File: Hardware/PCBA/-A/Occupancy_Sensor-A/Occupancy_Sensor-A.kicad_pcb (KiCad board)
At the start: 2 copper layers, 30 x 30 mm, 68 parts, among them J1 USB_C_Receptacle, J2 Conn_02x05_Odd_Even, Q1 2N7002, Q2 2N7002, Q3 2N7002, Q4 2N7002, Q5 2N7002, SW1 SW_Push, SW2 SW_SPDT, U1 TCS3430, U2 VL53L8CX, U4 STM32WB55CGUx, U6 ECMF02-2AMX6, U8 TPS7A03185PDQNR, U9 TPS7A0333PDBVR, Y2 Crystal_GND24_Small

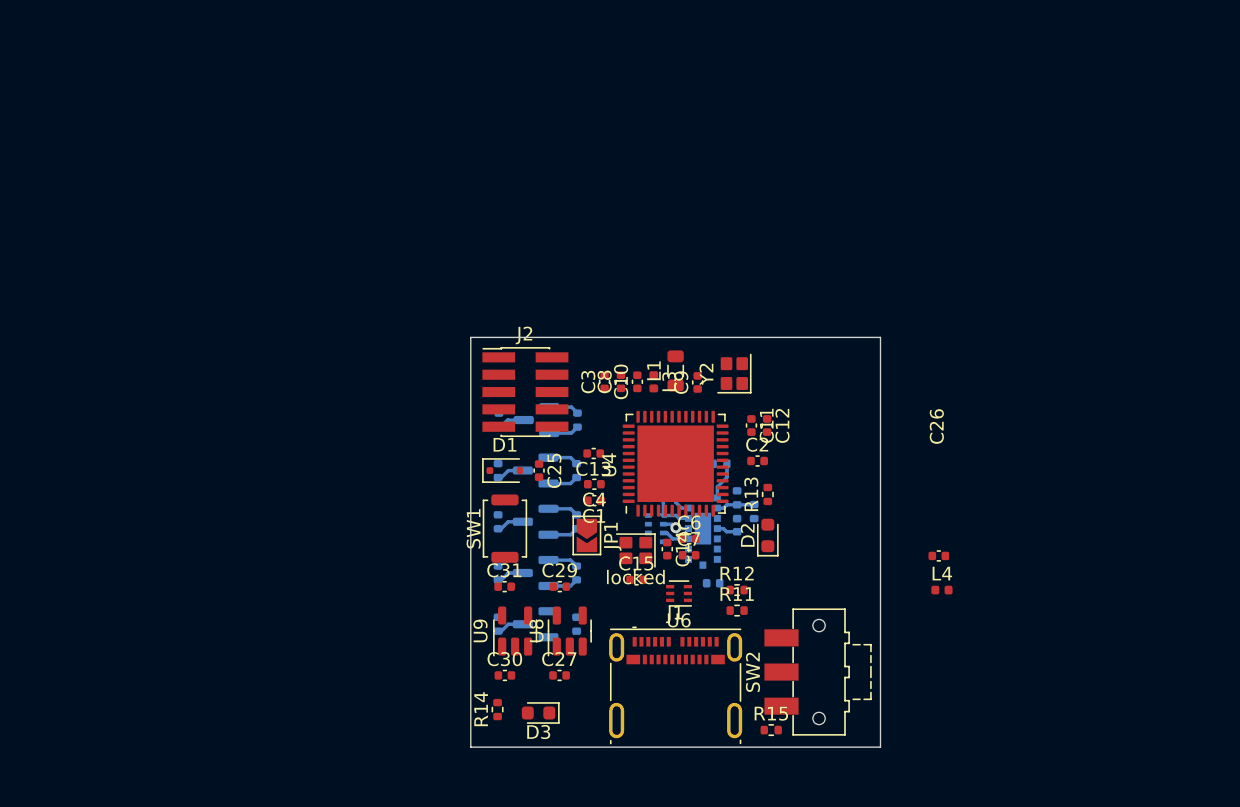
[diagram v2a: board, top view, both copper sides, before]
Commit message: General layout, footprint fixes
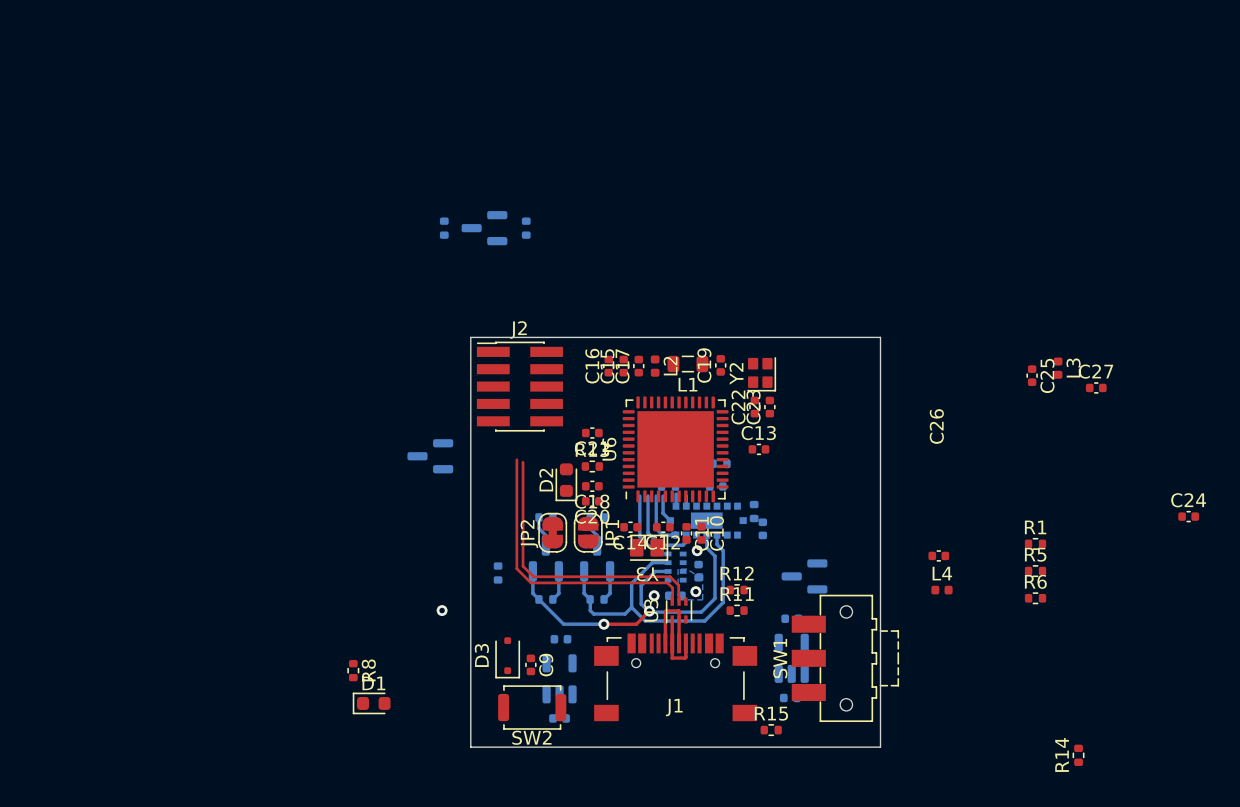
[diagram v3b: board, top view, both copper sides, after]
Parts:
- removed C29, C30, C31: 1u, Capacitor_SMD:C_0402_1005Metric
- removed R21, R22, R23, R24, R25: 2.2K, Resistor_SMD:R_0402_1005Metric
- removed U8: TPS7A03185PDQNR, Package_TO_SOT_SMD:SOT-23-5
- removed U9: TPS7A0333PDBVR, Package_TO_SOT_SMD:SOT-23-5
- removed locked: Crystal_GND24_Small, Crystal:Crystal_SMD_SeikoEpson_FA128-4Pin_2.0x1.6mm
- added C19: 4.7u, Capacitor_SMD:C_0402_1005Metric, F.Cu at (148.3, 102.0)
- added C20: 100n, Capacitor_SMD:C_0402_1005Metric, F.Cu at (138.9, 112.0)
- added C21: 100n, Capacitor_SMD:C_0402_1005Metric, F.Cu at (138.9, 107.0)
- added C22: 100n, Capacitor_SMD:C_0402_1005Metric, F.Cu at (150.8, 105.1)
- added C23: 100p, Capacitor_SMD:C_0402_1005Metric, F.Cu at (151.9, 105.1)
- added C24: 0.8pf, Capacitor_SMD:C_0402_1005Metric, F.Cu at (182.6, 113.1)
- added JP2: Jumper_2_Bridged, Jumper:SolderJumper-2_P1.3mm_Bridged_RoundedPad1.0x1.5mm, F.Cu at (136.0, 114.3)
- added L2: 10n, Inductor_SMD:L_0402_1005Metric, F.Cu at (143.5, 102.1)
- added R1: 5.1K, Resistor_SMD:R_0402_1005Metric, F.Cu at (171.3, 115.1)
- added R18: 2.2K, Resistor_SMD:R_0402_1005Metric, B.Cu at (139.2, 113.2)
- added R19: 2.2K, Resistor_SMD:R_0402_1005Metric, B.Cu at (135.5, 119.2)
- added R5: 47K, Resistor_SMD:R_0402_1005Metric, F.Cu at (171.3, 117.1)
- added R6: 47K, Resistor_SMD:R_0402_1005Metric, F.Cu at (171.3, 119.1)
- added U3: ECMF02-2AMX6, Package_DFN_QFN:ST_UQFN-6L_1.5x1.7mm_P0.5mm, F.Cu at (145.2, 120.0)
- added U5: TCS3430, Occupancy_Sensor_Custom_Footprints:TCS3430, B.Cu at (145.0, 116.8)
- added Y3: NX2012_32K768, Occupancy_Sensor_Custom_Footprints:NX2012_32K768, F.Cu at (142.9, 115.4)
- C1: value 100n -> 4.7u; moved to B.Cu
- C10: value 100n -> 1u
- C11: value 100n -> 10n
- C12: value 100p -> 10p
- C13: value 100n -> 4.7u
- C15: value 10p -> 4.7u
- C16, C17: moved to F.Cu
- C18: value 1u -> 100n; moved to F.Cu
- C2, C6: moved to B.Cu
- C25: value 100n -> 0.3pf
- C26: value C_Small -> 10nf
- C27: value 1u -> 1.2pf
- C3: value 100n -> 1u; moved to B.Cu
- C4: value 4.7u -> 100n; moved to B.Cu
- C5: value 4.7u -> 1u
- C7: value 10n -> 1u; moved to B.Cu
- C8: value 4.7u -> 1u; moved to B.Cu
- C9: value 4.7u -> 100n
- D1: value BAT54J -> LED; footprint Diode_SMD:D_SOD-323F -> LED_SMD:LED_0603_1608Metric
- D3: value LED -> BAT54J; footprint LED_SMD:LED_0603_1608Metric -> Diode_SMD:D_SOD-323F
- J1: footprint Connector_USB:USB_C_Receptacle_Molex_105450-0101 -> Occupancy_Sensor_Custom_Footprints:TYPEC-304S-ACP16
- JP1: footprint Jumper:SolderJumper-2_P1.3mm_Open_TrianglePad1.0x1.5mm -> Jumper:SolderJumper-2_P1.3mm_Open_RoundedPad1.0x1.5mm
- R10, R3: value 40K -> 47K
- R11: value 5.1K -> 40K
- R12: value 5.1K -> 47K
- R14: value 1K -> 2.2K
- R16, R17: value 47K -> 2.2K
- R2: value 47K -> 5.1K
- R4: value 47K -> 40K
- R8: value 47K -> 1K; moved to F.Cu
- SW1: value SW_Push -> SW_SPDT; footprint Button_Switch_SMD:SW_Push_SPST_NO_Alps_SKRK -> Button_Switch_SMD:SW_SPDT_CK-JS102011SAQN
- SW2: value SW_SPDT -> SW_Push; footprint Button_Switch_SMD:SW_SPDT_CK-JS102011SAQN -> Button_Switch_SMD:SW_Push_SPST_NO_Alps_SKRK
- U1: value TCS3430 -> TPS7A0333PDBVR; footprint Occupancy_Sensor_Custom_Footprints:TCS3430 -> Package_TO_SOT_SMD:SOT-23-5
- U4: value STM32WB55CGUx -> TPS7A03185PDQNR; footprint Package_DFN_QFN:QFN-48-1EP_7x7mm_P0.5mm_EP5.6x5.6mm -> Package_TO_SOT_SMD:SOT-23-5; moved to B.Cu
- U6: value ECMF02-2AMX6 -> STM32WB55CGUx; footprint Package_DFN_QFN:ST_UQFN-6L_1.5x1.7mm_P0.5mm -> Package_DFN_QFN:QFN-48-1EP_7x7mm_P0.5mm_EP5.6x5.6mm
- Y2: value Crystal_GND24_Small -> NX2016SA_32M; footprint Crystal:Crystal_SMD_SeikoEpson_FA128-4Pin_2.0x1.6mm -> Occupancy_Sensor_Custom_Footprints:NX2016SA_32M
- moved C27 44.6 mm to (175.8, 103.7)
- moved R14 42.7 mm to (174.5, 130.6)
- moved C25 36.8 mm to (171.1, 102.8)
- moved L3 29.6 mm to (173.0, 102.2)
- moved R7 29.2 mm to (134.1, 92.0)
- moved R10 29.1 mm to (128.1, 92.0)
- moved SW1 26.7 mm to (157.5, 123.5)
- moved C3 24.9 mm to (136.5, 127.9), turned to 0 degrees
- moved C9 24.0 mm to (134.4, 124.0), turned to -90 degrees
- moved SW2 21.2 mm to (134.5, 127.1), turned to 180 degrees
- moved Q3 20.0 mm to (154.4, 117.5)
- moved D1 19.6 mm to (122.9, 126.8)
- moved C17 16.8 mm to (142.3, 102.1), turned to 90 degrees
- moved U4 16.6 mm to (153.5, 123.5)
- moved C8 16.2 mm to (145.0, 118.9), turned to 0 degrees
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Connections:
- C1 pad 1: VDD -> +3.3V
- C10 pad 1: VDD -> VDD_ANALOG
- C11 pad 1: VDD -> VDD_ANALOG
- C12 pad 1: VDD -> GND
- C12 pad 2: GND -> /OSC32_OUT
- C13 pad 1: VDD_USB -> +3.3V
- C14 pad 1: GND -> /OSC32_IN
- C14 pad 2: /OSC32_OUT -> GND
- C15 pad 1: /OSC32_OUT -> +3.3V
- C16 pad 1: +1V8 -> +3.3V
- C17 pad 1: +1V8 -> +3.3V
- C18 pad 1: +1V8 -> +3.3V
- C2 pad 1: VDD -> +1V8
- C25 pad 1: NRST -> Net-(C25-Pad1)
- C26 pad 1: unconnected-(C26-Pad1) -> Net-(C26-Pad1)
- C26 pad 2: unconnected-(C26-Pad2) -> Net-(C26-Pad2)
- C27 pad 1: VBUS -> Net-(AE1-A)
- C3 pad 1: VDD -> VBUS
- C4 pad 1: VDD -> +1V8
- C6 pad 1: VDD_ANALOG -> VBUS
- C7 pad 1: VDD_ANALOG -> +1V8
- C8 pad 1: VDD -> +1V8
- C9 pad 1: Net-(U4-VFBSMPS) -> NRST
- D1 pad 1: Net-(D1-K) -> GND
- D1 pad 2: NRST -> Net-(D1-A)
- D3 pad 1: GND -> Net-(D3-K)
- D3 pad 2: Net-(D3-A) -> NRST
- J1 pad A6: Net-(U6-D+_in) -> Net-(U3-D+_in)
- J1 pad A7: Net-(U6-D-_in) -> Net-(U3-D-_in)
- J1 pad B6: Net-(U6-D+_in) -> Net-(U3-D+_in)
- J1 pad B7: Net-(U6-D-_in) -> Net-(U3-D-_in)
- JP1 pad 1: VDD -> +3.3V
- L1 pad 1: Net-(U4-VFBSMPS) -> Net-(U6-VFBSMPS)
- Q1 pad 2: /INT_CLR_1V8 -> /INT_TOF_1V8
- Q1 pad 3: /INT_CLR -> /INT_TOF
- Q2 pad 2: /SCL_1V8 -> /SYNC_1V8
- Q2 pad 3: /SCL_3V3 -> /SYNC_3V3
- Q3 pad 2: /SYNC_1V8 -> /INT_CLR_1V8
- Q3 pad 3: /SYNC_3V3 -> /INT_CLR
- Q4 pad 2: /SDA_1V8 -> /SCL_1V8
- Q4 pad 3: /SDA_3V3 -> /SCL_3V3
- Q5 pad 2: /INT_TOF_1V8 -> /SDA_1V8
- Q5 pad 3: /INT_TOF -> /SDA_3V3
- R10 pad 1: /I2C_RST -> +3.3V
- R10 pad 2: /I2C_RST_1V8 -> /SYNC_3V3
- R11 pad 1: Net-(J1-CC1) -> /LPn
- R11 pad 2: GND -> /LPn_1V8
- R12 pad 1: Net-(J1-CC2) -> /LPn_1V8
- R14 pad 1: Net-(D3-A) -> +1V8
- R14 pad 2: VBUS -> /INT_CLR_1V8
- R15 pad 1: Net-(SW2-B) -> Net-(SW1-B)
- R16 pad 2: /INT_TOF_1V8 -> /SCL_1V8
- R17 pad 2: /INT_TOF -> /INT_CLR
- R2 pad 1: Net-(U2-SPI_I2C_N) -> Net-(J1-CC2)
- R20 pad 1: +1V8 -> +3.3V
- R20 pad 2: /INT_CLR_1V8 -> /SDA_3V3
- R3 pad 1: /LPn -> Net-(U2-SPI_I2C_N)
- R3 pad 2: /LPn_1V8 -> GND
- R4 pad 1: /LPn_1V8 -> /I2C_RST
- R4 pad 2: GND -> /I2C_RST_1V8
- R8 pad 1: +3.3V -> Net-(D1-A)
- R8 pad 2: /SYNC_3V3 -> VBUS
- R9 pad 1: /I2C_RST_1V8 -> +3.3V
- R9 pad 2: GND -> /INT_TOF
- SW1 pad 1: GND -> +3.3V
- SW1 pad 2: Net-(D1-K) -> Net-(SW1-B)
- SW2 pad 1: +3.3V -> GND
- SW2 pad 2: Net-(SW2-B) -> Net-(D3-K)
- U1 pad 1: +1V8 -> VBUS
- U1 pad 2: /SDA_1V8 -> GND
- U1 pad 3: /SCL_1V8 -> VBUS
- U1 pad 4: /INT_CLR_1V8 -> unconnected-(U1-NC-Pad4)
- U1 pad 5: unconnected-(U1-N/C-Pad5) -> +3.3V
- U4 pad 1: Net-(JP1-B) -> VBUS
- U4 pad 2: /OSC32_IN -> GND
- U4 pad 3: /OSC32_OUT -> /1V8_EN
- U4 pad 4: BOOT -> unconnected-(U4-NC-Pad4)
- U4 pad 5: /PB8 -> +1V8
- U6 pad 1: Net-(U6-D+_in) -> Net-(JP1-B)
- U6 pad 2: Net-(U6-D-_in) -> /OSC32_IN
- U6 pad 3: GND -> /OSC32_OUT
- U6 pad 4: unconnected-(U6-NC-Pad4) -> BOOT
- U6 pad 5: USB_N -> /PB8
- U6 pad 6: USB_P -> /PB9
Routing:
- net /SDA_1V8: track 4.28 -> 26.2 mm, vias 1 -> 3
- net USB_P: track 0.00 -> 21.0 mm
- net USB_N: track 0.00 -> 20.8 mm
- net /SCL_1V8: track 4.27 -> 24.2 mm
- net +1V8: track 13.3 -> 4.49 mm, vias 0 -> 2
- net Net-(U3-D-_in): track 0.00 -> 5.72 mm
- net Net-(U3-D+_in): track 0.00 -> 4.88 mm
- net /INT_CLR_1V8: track 2.24 -> 5.58 mm
- net /I2C_RST_1V8: track 2.81 -> 0.74 mm
- net /SYNC_3V3: track 2.02 -> 0.00 mm
- net /INT_TOF: track 2.02 -> 0.00 mm
- net /INT_CLR: track 2.02 -> 0.00 mm
- net /SYNC_1V8: track 0.00 -> 2.02 mm
- net Net-(U2-SPI_I2C_N): track 2.79 -> 0.89 mm
- net +3.3V: track 1.54 -> 0.00 mm
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- added copper zone on B.Cu, net GND
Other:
- copper layers 2 -> 4

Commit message: Layout, power planes, prelim antenna placement
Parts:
- added REF**: Texas_SWRA117D_2.4GHz_Right, RF_Antenna:Texas_SWRA117D_2.4GHz_Right, F.Cu at (154.3, 117.5)
- R14, R5, R6: moved to B.Cu
- R2: moved to F.Cu
- moved R14 36.6 mm to (139.8, 119.1), turned to 180 degrees
- moved R6 31.9 mm to (144.1, 102.6), turned to 90 degrees
- moved R1 30.0 mm to (141.8, 120.5), turned to 180 degrees
- moved C24 28.8 mm to (153.8, 111.0), turned to 180 degrees
- moved R5 26.9 mm to (145.3, 110.4), turned to 90 degrees
- moved R10 26.4 mm to (150.1, 106.4), turned to 90 degrees
- moved C27 22.6 mm to (154.9, 112.3)
- moved Q2 21.7 mm to (147.2, 106.4), turned to 0 degrees
- moved Q1 21.0 mm to (147.2, 102.7), turned to 0 degrees
- moved L3 20.0 mm to (154.3, 109.4), turned to 90 degrees
- moved C25 18.0 mm to (153.8, 107.8), turned to 180 degrees
- moved SW1 17.7 mm to (160.3, 106.0)
- moved R7 17.6 mm to (144.1, 106.4), turned to 90 degrees
- moved C6 15.6 mm to (137.9, 128.4)
- moved C7 15.6 mm to (138.0, 122.6)
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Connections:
- Q1 pad 3: /INT_TOF -> INT_TOF_3V3
- Q2 pad 3: /SYNC_3V3 -> SYNC_3V3
- Q4 pad 3: /SCL_3V3 -> SCL_3V3
- Q5 pad 3: /SDA_3V3 -> SDA_3V3
- R10 pad 2: /SYNC_3V3 -> SYNC_3V3
- R18 pad 2: /SCL_3V3 -> SCL_3V3
- R20 pad 2: /SDA_3V3 -> SDA_3V3
- R4 pad 1: /I2C_RST -> I2C_RST
- R9 pad 2: /INT_TOF -> INT_TOF_3V3
- U6 pad 15: /PA6 -> INT_TOF_3V3
- U6 pad 16: /PA7 -> SYNC_3V3
- U6 pad 17: /PA8 -> I2C_RST
- U6 pad 46: /PB6 -> SCL_3V3
- U6 pad 47: /PB7 -> SDA_3V3
- U6 pad 8: VDD_ANALOG -> unconnected-(U6-VDDA-Pad8)
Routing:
- net +1V8: track 4.49 -> 53.5 mm, vias 2 -> 4
- net NRST: track 0.00 -> 26.1 mm
- net +3.3V: track 0.00 -> 20.7 mm, vias 0 -> 4
- net unconnected-(J1-SHIELD-PadS1): track 0.00 -> 18.5 mm
- net USB_N: track 20.8 -> 36.2 mm, vias 0 -> 2
- net USB_P: track 21.0 -> 35.7 mm, vias 0 -> 2
- net INT_TOF_3V3: track 0.00 -> 14.7 mm, vias 0 -> 1
- net /INT_TOF_1V8: track 3.99 -> 17.5 mm
- net SCL_3V3: track 0.00 -> 13.3 mm, vias 0 -> 1
- net SDA_3V3: track 0.00 -> 12.1 mm, vias 0 -> 1
- net GND: track 0.00 -> 11.0 mm, vias 1 -> 5
- net SYNC_3V3: track 0.00 -> 10.3 mm, vias 0 -> 1
- net SWCLK: track 0.00 -> 10.1 mm
- net /SYNC_1V8: track 2.02 -> 11.8 mm
- net SWO: track 0.00 -> 9.65 mm
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- added copper zone on F.Cu, net +3.3V
- added copper zone on In2.Cu, net +3.3V
- added copper zone on F.Cu, net GND
- added copper zone on In1.Cu, net GND
- added copper zone on F.Cu, net VDD_ANALOG

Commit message: Finalize IO pinout, layout
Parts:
- removed REF**: Texas_SWRA117D_2.4GHz_Right, RF_Antenna:Texas_SWRA117D_2.4GHz_Right
- R11, R12: moved to B.Cu
- moved C7 20.3 mm to (157.9, 126.4), turned to 90 degrees
- moved U4 17.0 mm to (155.0, 125.9), turned to 0 degrees
- moved C6 14.8 mm to (152.1, 124.4), turned to 90 degrees
- moved R11 9.17 mm to (153.6, 111.8)
- moved R12 6.78 mm to (153.6, 113.1), turned to 180 degrees
- moved C3 5.52 mm to (137.9, 124.5), turned to 90 degrees
- moved C5 2.76 mm to (132.1, 124.5), turned to 90 degrees
- moved C2 1.20 mm to (151.2, 115.2)
- moved U1 1.08 mm to (135.0, 125.9), turned to 180 degrees
- moved C21 0.35 mm to (138.7, 105.3)
- turned R18 to 180 degrees
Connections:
- net /SCL_1V8 renamed SCL_1V8
- net /SDA_1V8 renamed SDA_1V8
- Q3 pad 3: /INT_CLR -> INT_CLR_3V3
- R11 pad 1: /LPn -> LPn_3V3
- R17 pad 2: /INT_CLR -> INT_CLR_3V3
- U6 pad 14: /PA5 -> LPn_3V3
- U6 pad 42: /PA15 -> INT_CLR_3V3
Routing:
- net +1V8: track 53.5 -> 86.7 mm, vias 4 -> 12
- net NRST: track 26.1 -> 58.2 mm, vias 0 -> 2
- net /LPn_1V8: track 8.99 -> 40.1 mm
- net INT_CLR_3V3: track 0.00 -> 15.3 mm, vias 0 -> 1
- net Net-(JP2-B): track 3.20 -> 18.4 mm, vias 0 -> 2
- net VBUS: track 0.00 -> 12.5 mm, vias 0 -> 7
- net +3.3V: track 20.7 -> 28.6 mm, vias 4 -> 13
- net LPn_3V3: track 0.00 -> 5.21 mm, vias 0 -> 1
- net /PA5: track 3.42 -> 0.00 mm, vias 1 -> 0
- net /INT_CLR: track 3.39 -> 0.00 mm
- net /PA3: track 6.16 -> 4.66 mm
- net SWO: track 9.65 -> 11.1 mm
- net USB_P: track 35.7 -> 36.9 mm
- net SCL_3V3: track 13.3 -> 14.4 mm
- net GND: track 11.0 -> 11.6 mm, vias 5 -> 15
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- added copper zone on B.Cu, net +1V8
- added copper zone on B.Cu, net +3.3V
- added copper zone on B.Cu, net VBUS
- added copper zone on F.Cu, net VBUS

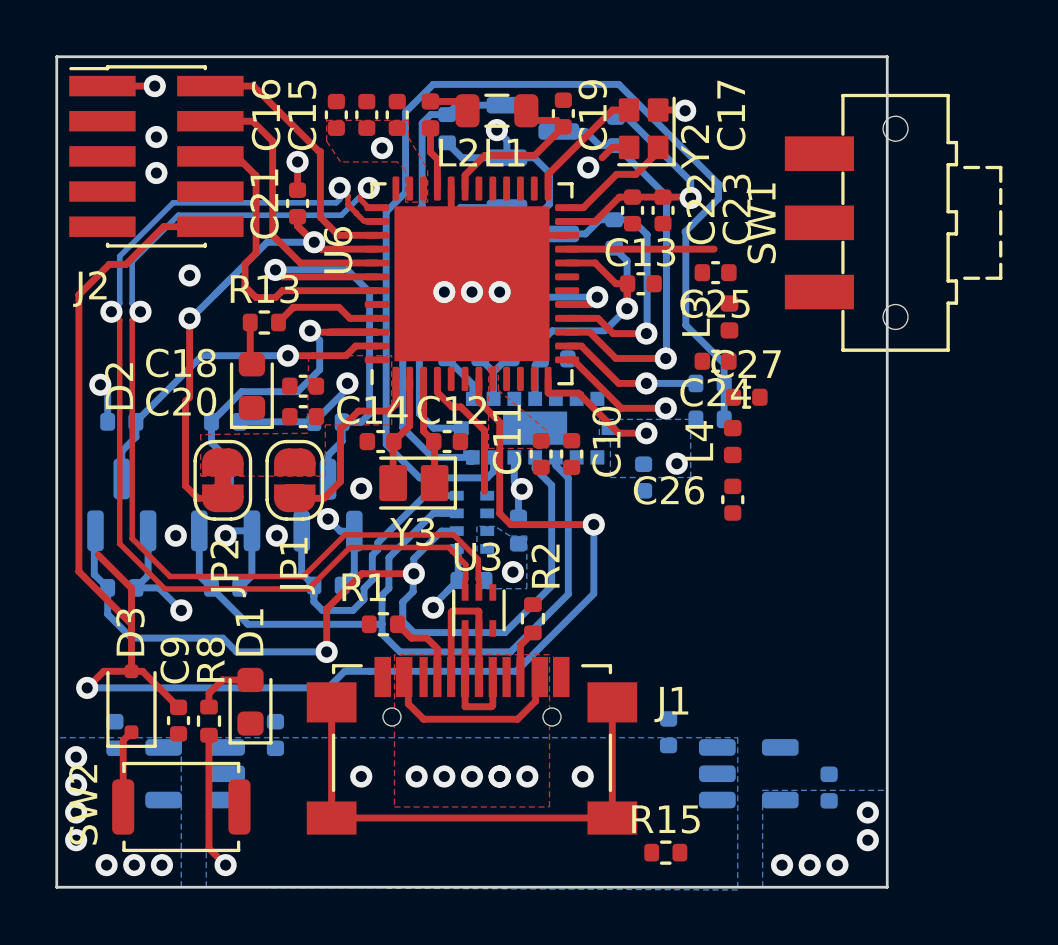
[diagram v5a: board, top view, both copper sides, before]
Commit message: Layout cleanup, silk fixes
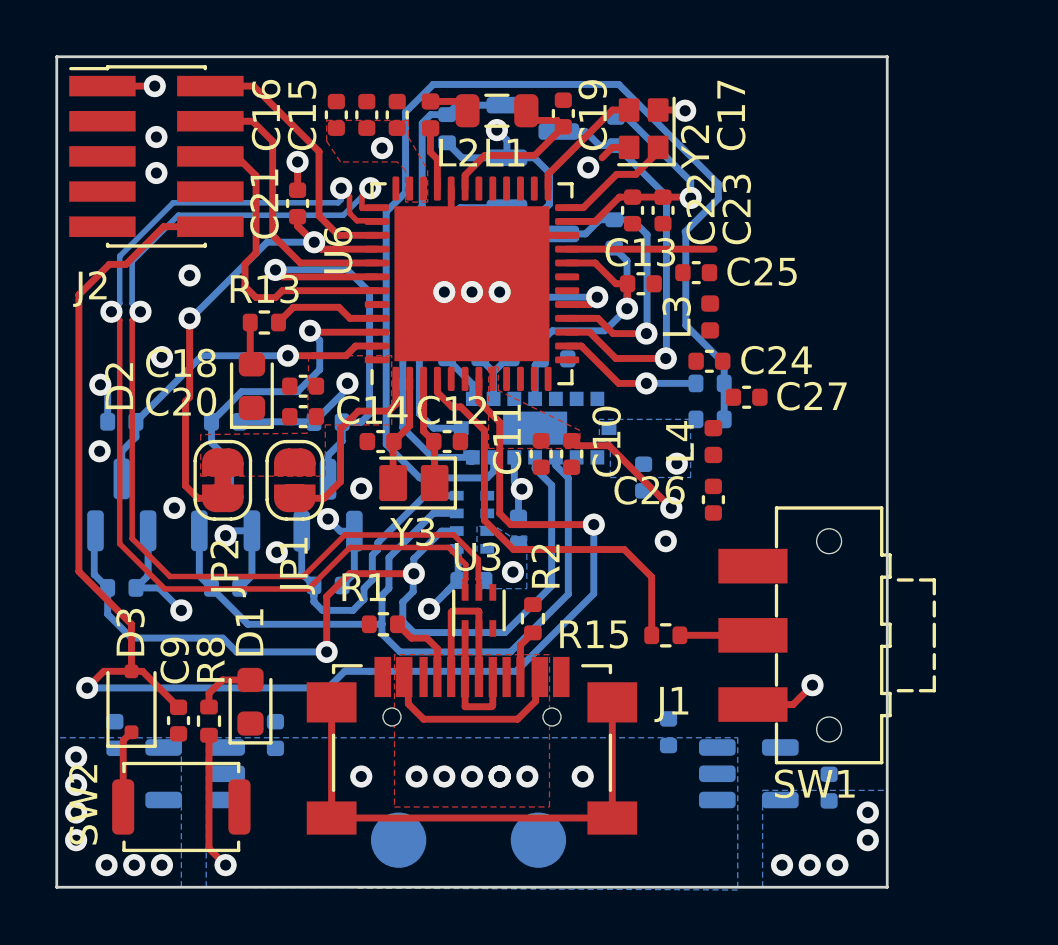
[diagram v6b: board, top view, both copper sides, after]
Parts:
- added TP1: 5V, TestPoint:TestPoint_Pad_D2.0mm, B.Cu at (142.3, 128.3)
- added TP2: GND, TestPoint:TestPoint_Pad_D2.0mm, B.Cu at (147.4, 128.3)
- moved SW1 15.1 mm to (157.9, 120.9)
- moved R15 7.85 mm to (152.0, 120.9), turned to 180 degrees
- moved C25 0.70 mm to (153.1, 107.8)
- moved L3 0.70 mm to (153.6, 109.4)
- moved C26 0.70 mm to (153.7, 116.0)
- moved L4 0.70 mm to (153.7, 113.9)
- moved C24 0.23 mm to (153.6, 111.0)
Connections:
- C10 pad 1: VDD_ANALOG -> +3.3V
- C11 pad 1: VDD_ANALOG -> +3.3V
- U6 pad 8: unconnected-(U6-VDDA-Pad8) -> +3.3V
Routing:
- net BOOT: track 4.96 -> 15.0 mm
- net +3.3V: track 28.6 -> 35.6 mm, vias 13 -> 15
- net /PA3: track 4.66 -> 0.00 mm, vias 1 -> 0
- net /PA4: track 4.19 -> 0.21 mm, vias 1 -> 0
- net SCL_3V3: track 14.4 -> 10.9 mm
- net NRST: track 58.2 -> 55.2 mm
- net Net-(SW1-B): track 0.00 -> 2.64 mm
- net Net-(JP2-B): track 18.4 -> 17.7 mm
- net GND: vias 15 -> 18
- added copper zone on In2.Cu, net +1V8
- removed copper zone on F.Cu, net VDD_ANALOG
